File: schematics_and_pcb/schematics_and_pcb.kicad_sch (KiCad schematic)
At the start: 47 parts

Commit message: prettier lables
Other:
- note added: "MICRO CONTROLLER"
- note added: "SENSOR"
- note added: "SENSOR PSU"
- note removed: "MCU"
- note removed: "Sensor"
- note removed: "Sensor powersupply"
- moved on the sheet: 1v?, 3v?, 5v?, C?, J?, MCO?, MOTION?, PH?, SW?, gnd?

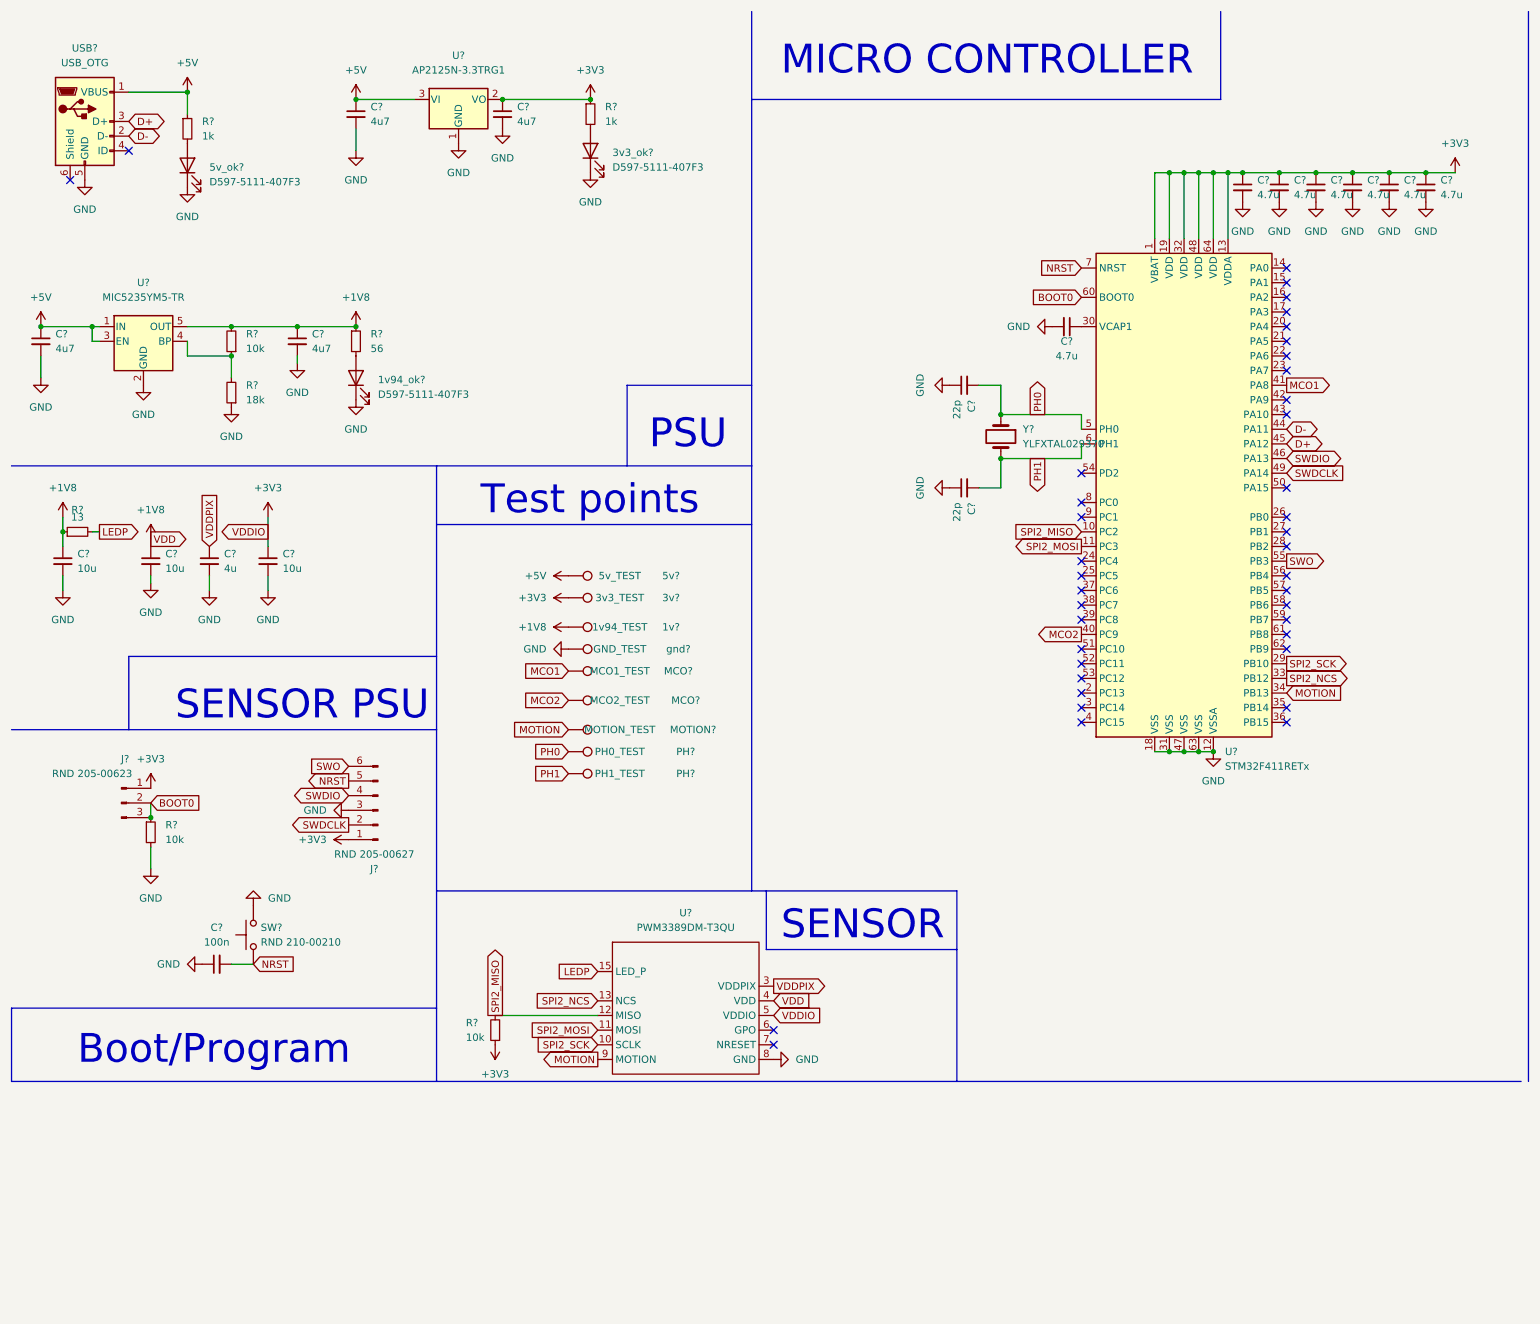
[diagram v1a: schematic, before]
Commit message: added left and right buttons
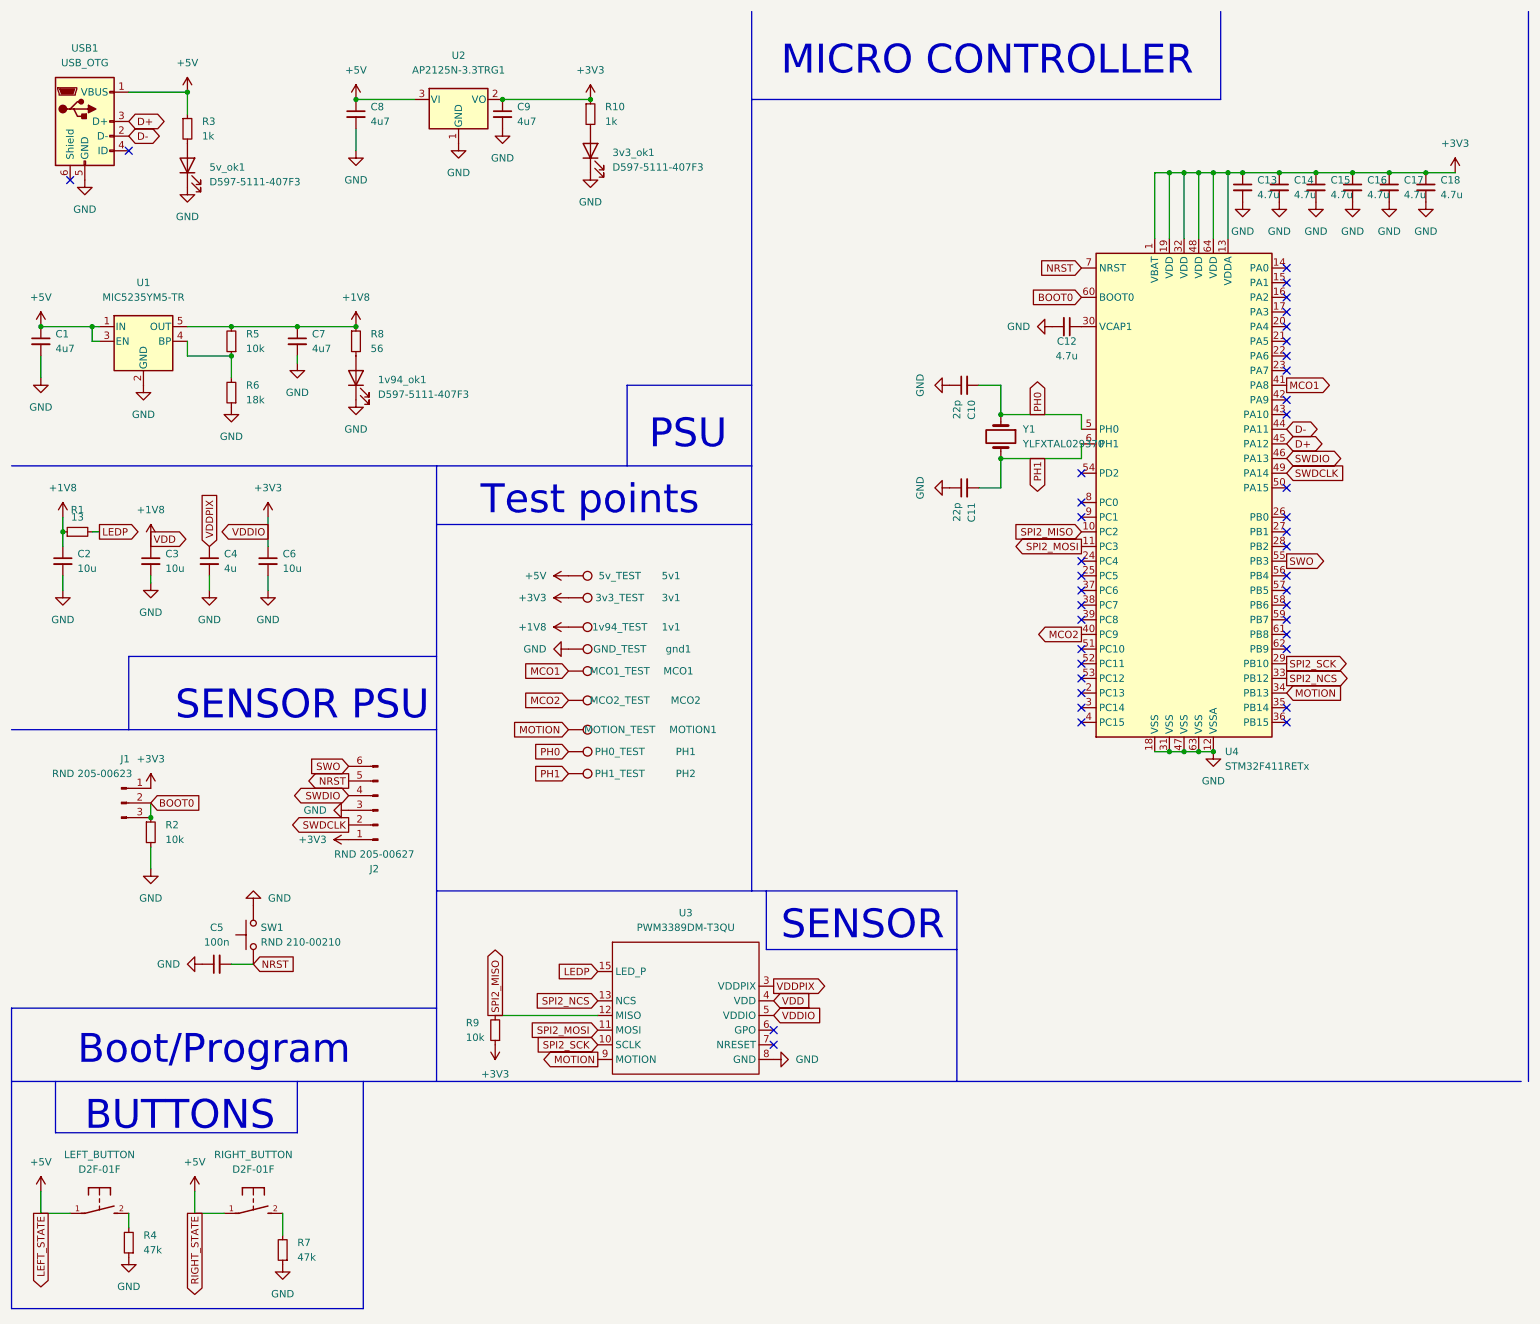
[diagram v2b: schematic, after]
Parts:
- added LEFT_BUTTON, RIGHT_BUTTON: D2F-01F, D2F-01F, symbol mouse:D2F-01F
- added R4, R7: 47k, symbol Device:R_Small
- gave numbers to parts that had none: 47
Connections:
- net +5V: now also LEFT_BUTTON.1, RIGHT_BUTTON.1
- net GND: now also R4.1, R7.1
- new net: R7.2, RIGHT_BUTTON.2
- new net: LEFT_BUTTON.2, R4.2
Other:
- note added: "BUTTONS"

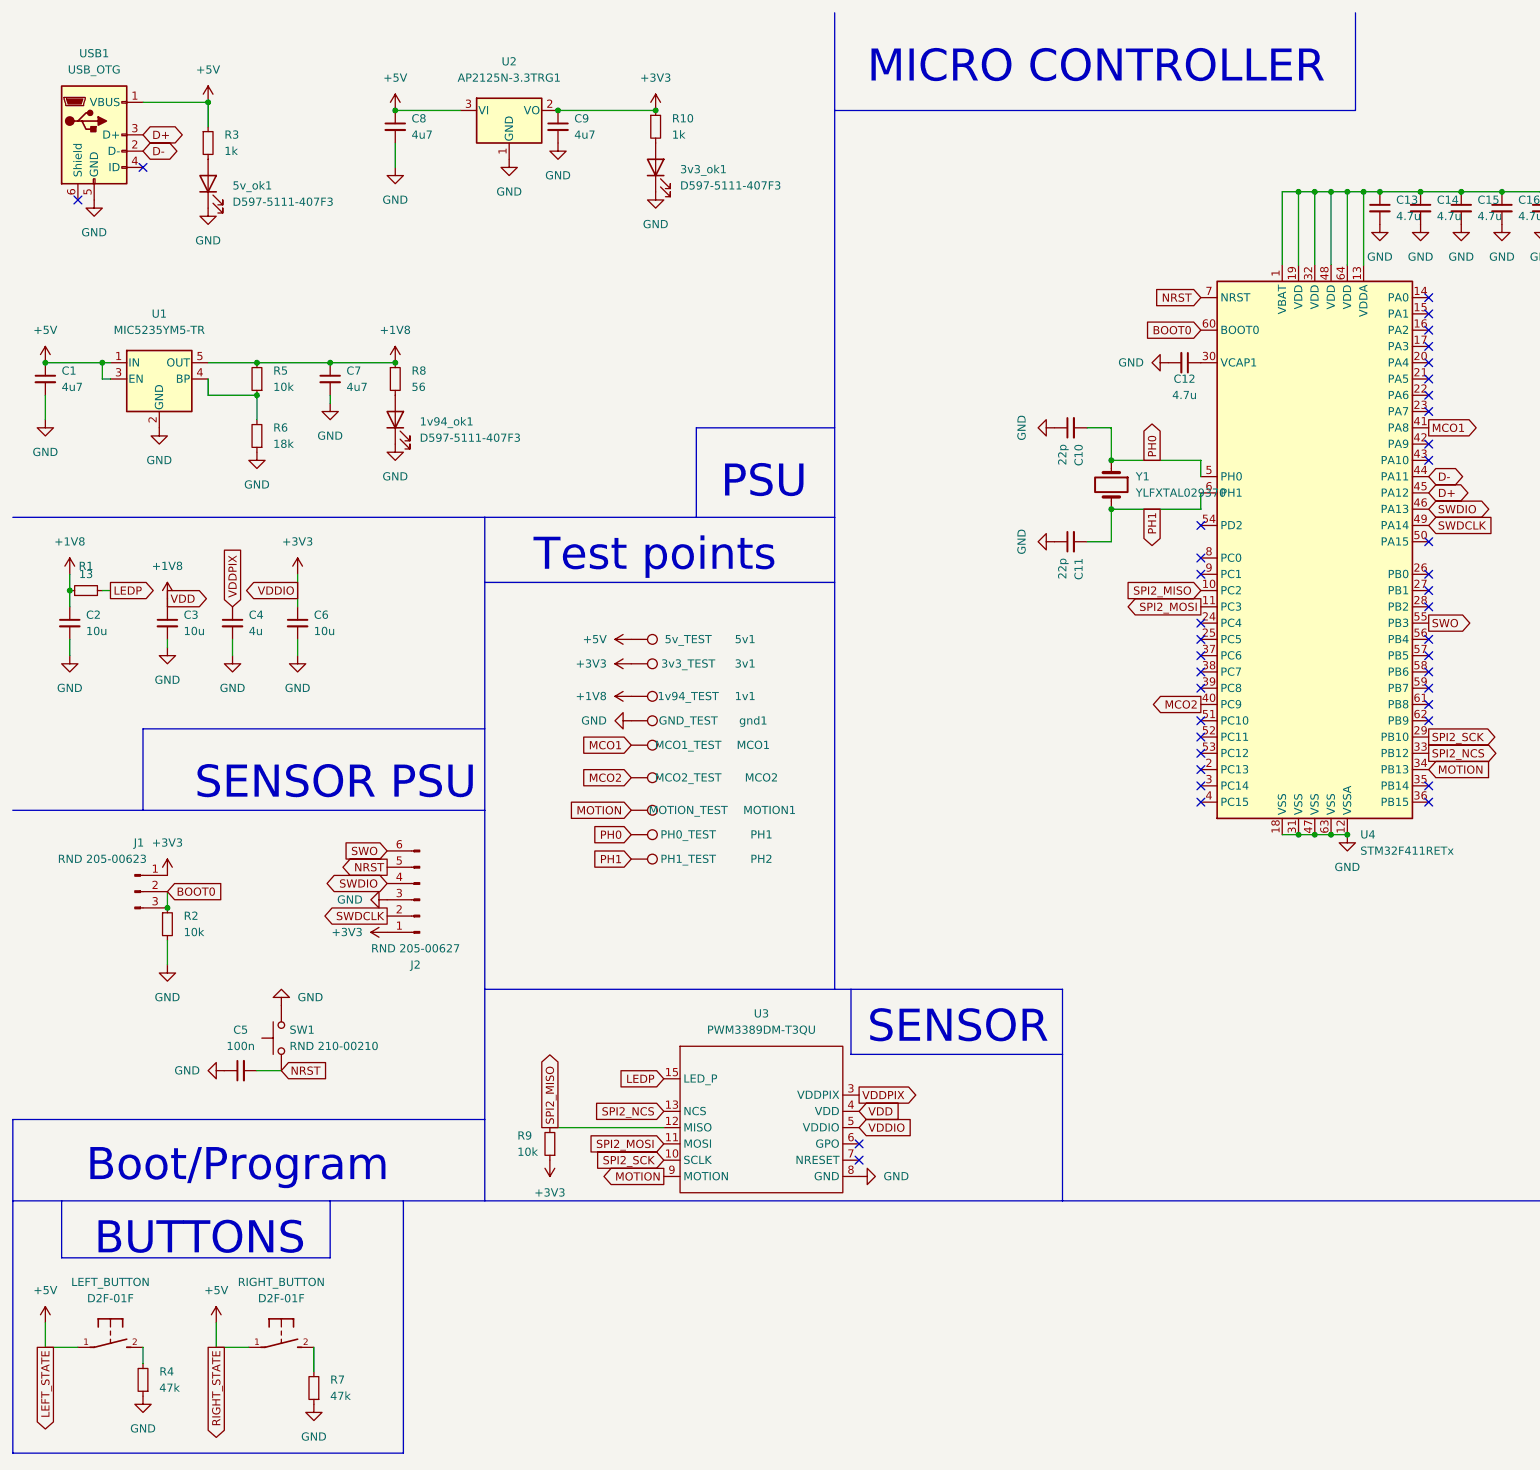
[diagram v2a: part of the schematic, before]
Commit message: added more buttons and scroll wheel
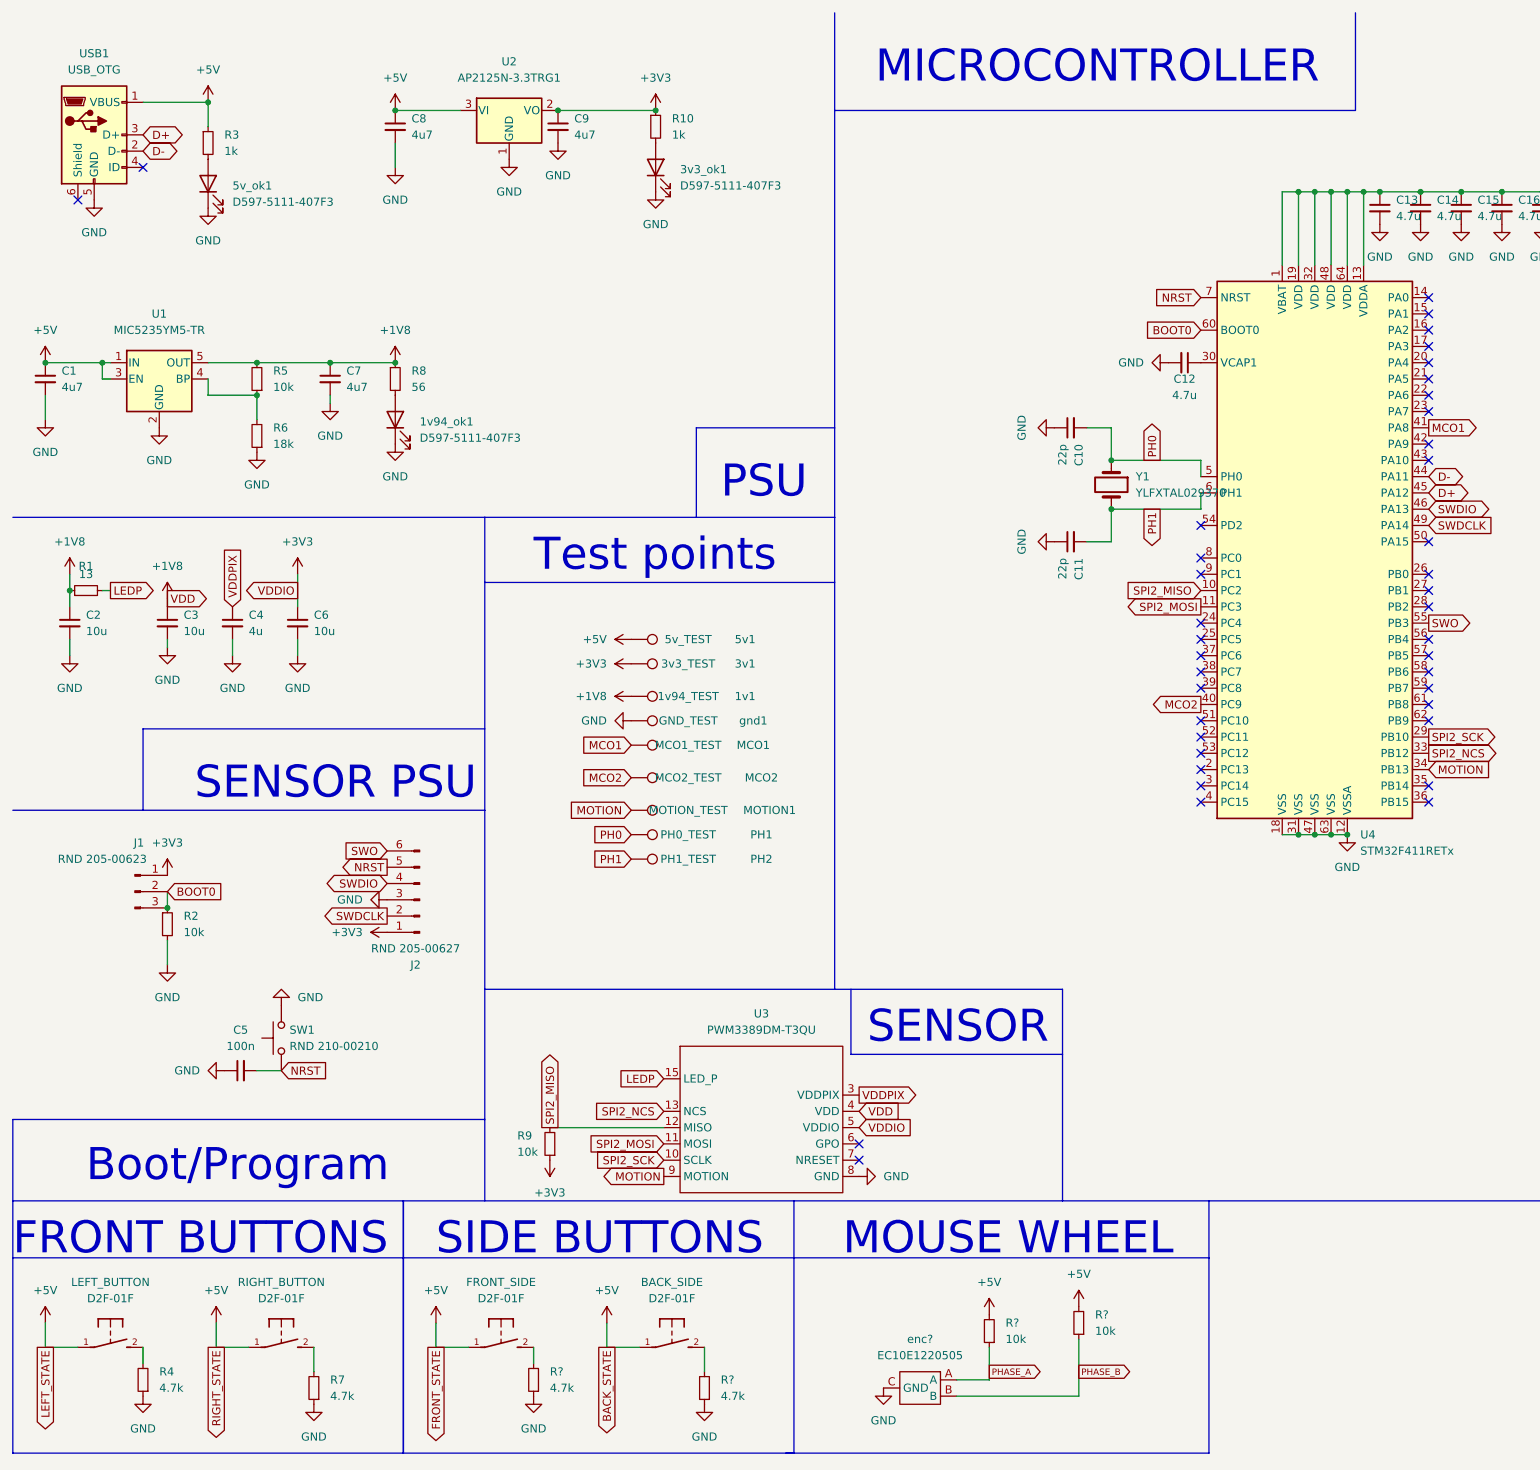
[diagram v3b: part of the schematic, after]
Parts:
- added BACK_SIDE, FRONT_SIDE: D2F-01F, D2F-01F, symbol mouse:D2F-01F
- added R? (x2): 4.7k, symbol Device:R_Small
- added R? (x2): 10k, symbol Device:R_Small
- added enc?: EC10E1220505, symbol mouse:EC10E1220505
- R4, R7: value 47k -> 4.7k
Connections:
- net +5V: now also BACK_SIDE.1, FRONT_SIDE.1, R?.2, R?.2
- net GND: now also R?.1, R?.1, enc?.C (GND)
- new net: FRONT_SIDE.2, R?.2
- new net: BACK_SIDE.2, R?.2
- new net PHASE_A: R?.1, enc?.A
- new net PHASE_B: R?.1, enc?.B
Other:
- note added: "FRONT BUTTONS"
- note added: "MICROCONTROLLER"
- note added: "MOUSE WHEEL"
- note added: "SIDE BUTTONS"
- note removed: "BUTTONS"
- note removed: "MICRO CONTROLLER"

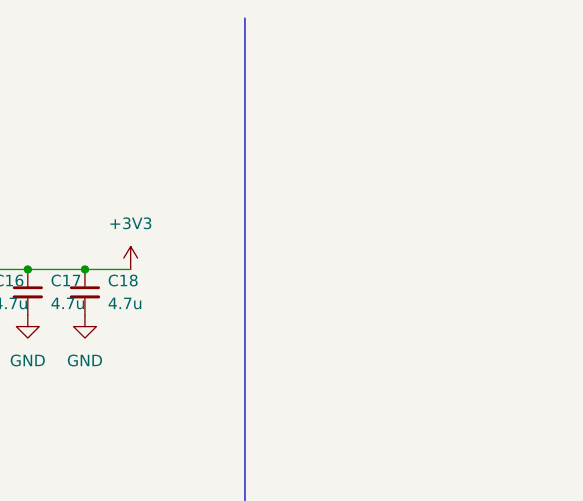
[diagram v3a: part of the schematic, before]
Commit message: added BOM
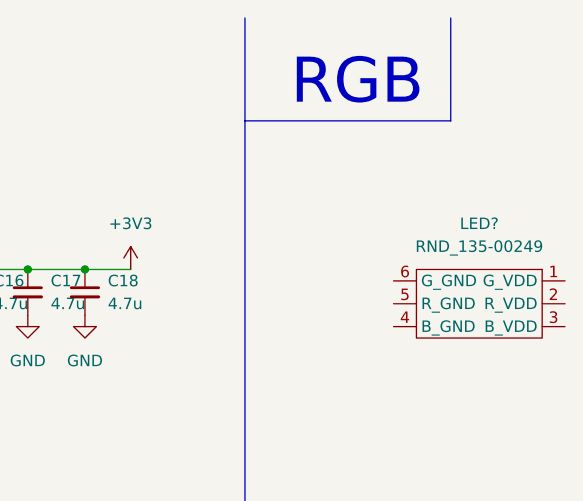
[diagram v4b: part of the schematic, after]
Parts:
- added LED?: RND_135-00249, symbol mouse:RND_135-00249
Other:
- note added: "RGB"
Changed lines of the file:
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@@
+    (stroke (width 0) (type default) (color 0 0 0 0))
+  )
+  (polyline (pts (xy 298.45 12.7) (xy 298.45 24.13))
     (stroke (width 0) (type default) (color 0 0 0 0))
   )
@@
   )
   (wire (pts (xy 57.15 110.49) (xy 57.15 113.03))
+    (stroke (width 0) (type default) (color 0 0 0 0))
+  )
+  (polyline (pts (xy 275.59 24.13) (xy 298.45 24.13))
     (stroke (width 0) (type default) (color 0 0 0 0))
   )
@@
   )
   (text "SENSOR" (at 146.05 173.99 0)
+    (effects (font (size 5 5)) (justify left bottom))
+  )
+  (text "RGB" (at 280.67 22.86 0)
     (effects (font (size 5 5)) (justify left bottom))
   )
@@
     )
     (pin "1")
+  )
+  (symbol (lib_id "mouse:RND_135-00249") (at 308.61 48.26 270) (unit 1)
+    (in_bom yes) (on_board yes) (fields_autoplaced)
+    (property "Reference" "LED?" (id 0) (at 301.625 35.56 90))
+    (property "Value" "RND_135-00249" (id 1) (at 301.625 38.1 90))
+    (property "Footprint" "" (id 2) (at 311.15 50.8 0)
+      (effects (font (size 1.27 1.27)) hide)
+    )
+    (property "Datasheet" "" (id 3) (at 311.15 50.8 0)
+      (effects (font (size 1.27 1.27)) hide)
+    )
+    (pin "1")
+    (pin "2")
+    (pin "3")
+    (pin "4")
+    (pin "5")
+    (pin "6")
   )
   (symbol (lib_id "power:+3V3") (at 262.89 40.64 0) (unit 1)
@@
       (reference "J2") (unit 1) (value "RND 205-00627") (footprint "Connector_PinHeader_2.54mm:PinHeader_1x06_P2.54mm_Vertical")
     )
+    (path "/798b3d00-69ee-43b8-a149-366f724b5aaa"
+      (reference "LED?") (unit 1) (value "RND_135-00249") (footprint "")
+    )
     (path "/fd975609-7adf-48bb-bc3e-84d8eed1717e"
